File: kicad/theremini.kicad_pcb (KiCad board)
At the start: 2 copper layers, 2 parts, among them U1 VL53L0CXV0DH/1, U2 VL53L0CXV0DH/1

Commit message: Add libraries
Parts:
- removed U1, U2: VL53L0CXV0DH/1, VL53L0CXV0DH1:OPTO-SMD_12P_VL53L0CXV0DH-1
- added U3: STM32L432KBUx, Package_DFN_QFN:QFN-32-1EP_5x5mm_P0.5mm_EP3.45x3.45mm, F.Cu at (3.15, 3.15)

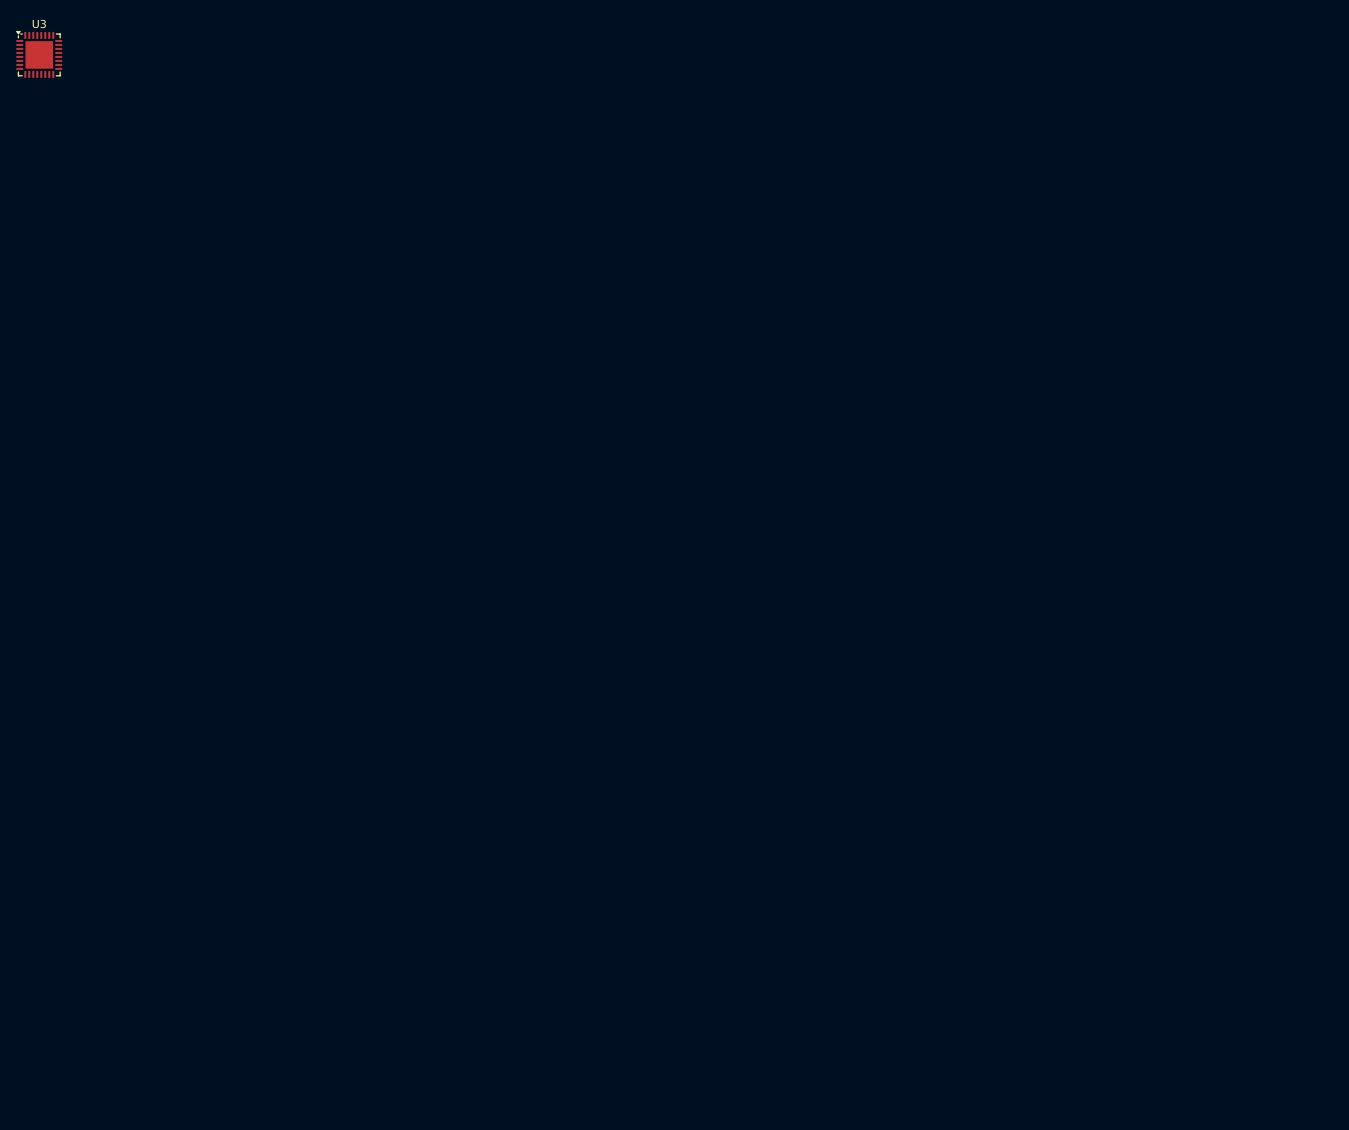
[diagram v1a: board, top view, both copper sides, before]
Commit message: Place footprints
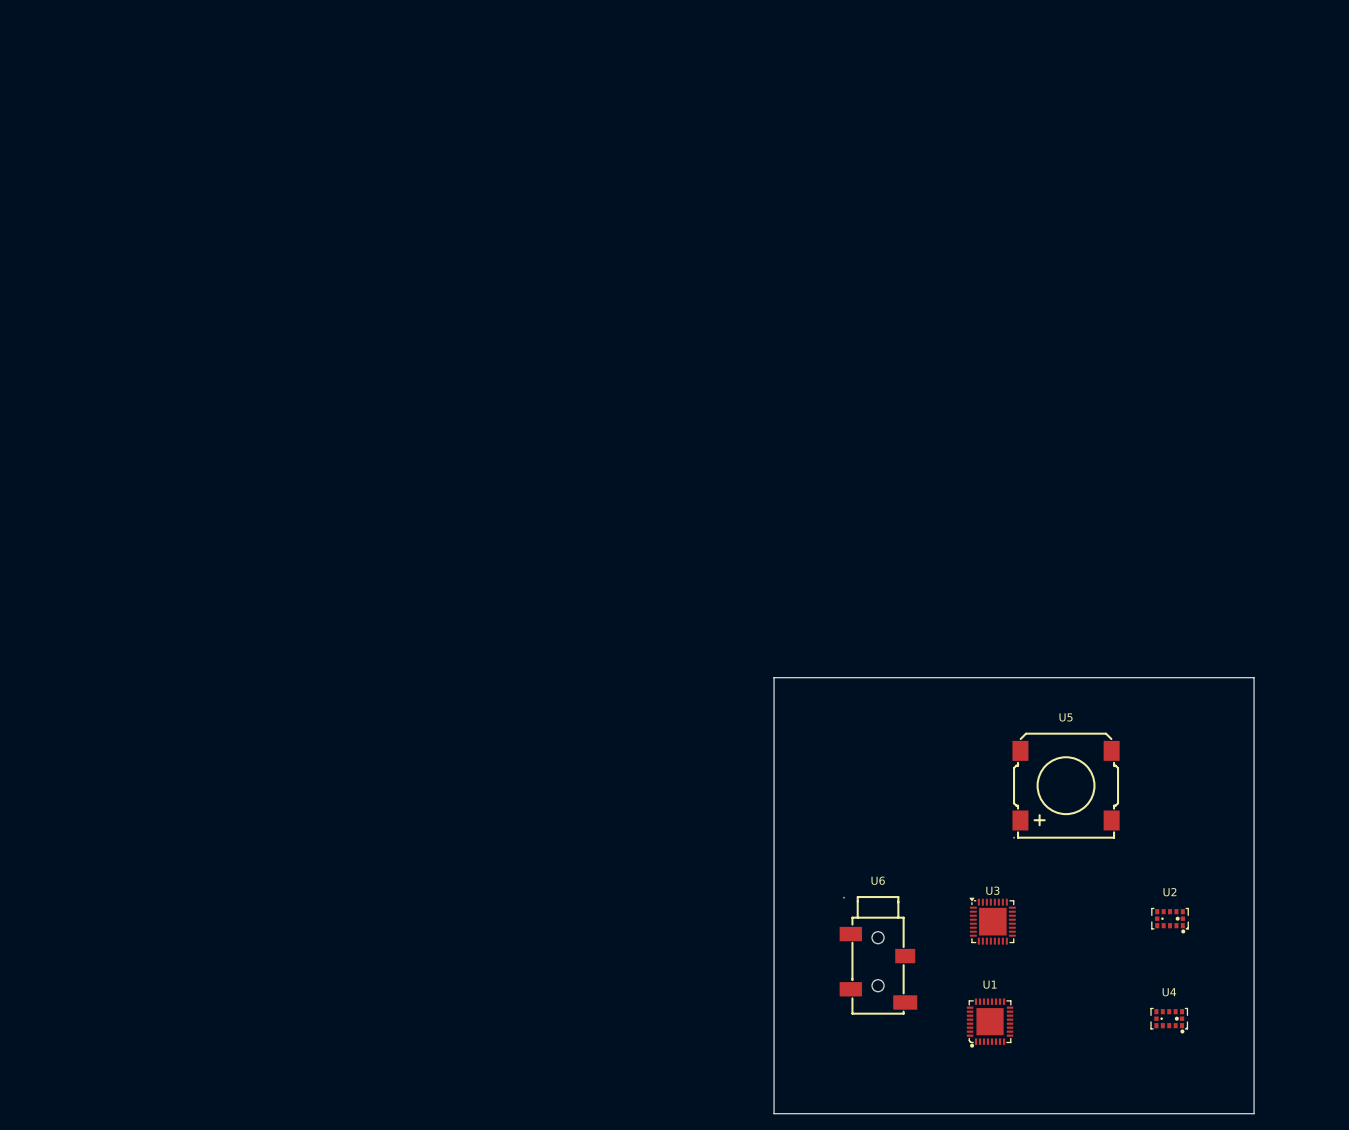
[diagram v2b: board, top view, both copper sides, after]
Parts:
- added U1: NAU88C22YG, NAU88C22YG:QFN-32_L5.0-W5.0-P0.50-BL-EP3.4, F.Cu at (122.0, 124.0)
- added U2: VL53L0CXV0DH/1, VL53L0CXV0DH1:OPTO-SMD_12P_VL53L0CXV0DH-1, F.Cu at (144.5, 111.1)
- added U4: VL53L0CXV0DH/1, VL53L0CXV0DH1:OPTO-SMD_12P_VL53L0CXV0DH-1, F.Cu at (144.4, 123.6)
- added U5: KLJ-01304T-08R07W, KLJ-01304T-08R07W:BUZ-SMD_4P-L13.0-W13.0-P11.4-BL, F.Cu at (131.5, 94.5)
- added U6: PJ-327C-4A, PJ-327C-4A:AUDIO-SMD_PJ-327C-4A, F.Cu at (108.0, 117.3)
- moved U3 161.1 mm to (122.3, 111.5)
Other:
- board outline added: 60 x 54.5 mm

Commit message: added things
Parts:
- removed U3: STM32L432KBUx, Package_DFN_QFN:QFN-32-1EP_5x5mm_P0.5mm_EP3.45x3.45mm
- added U7: STM32L432KBU6TR, STM32L432KBU6TR:UFQFPN-32_L5.0-W5.0-P0.50-TL-EP3.5, F.Cu at (123.0, 110.7)

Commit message: Connected things
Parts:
- added C1: 10u, Capacitor_SMD:C_0402_1005Metric, F.Cu at (100.7, 85.9)
- added C10: 100n, Capacitor_SMD:C_0402_1005Metric, F.Cu at (108.7, 88.4)
- added C11: 100n, Capacitor_SMD:C_0402_1005Metric, F.Cu at (108.7, 90.9)
- added C12: 15p, Capacitor_SMD:C_0402_1005Metric, F.Cu at (108.7, 93.4)
- added C2: 10u, Capacitor_SMD:C_0402_1005Metric, F.Cu at (100.7, 88.4)
- added C3: 10u, Capacitor_SMD:C_0402_1005Metric, F.Cu at (100.7, 90.9)
- added C4: 1n, Capacitor_SMD:C_0402_1005Metric, F.Cu at (100.7, 93.4)
- added C5: 4u7, Capacitor_SMD:C_0402_1005Metric, F.Cu at (104.7, 85.9)
- added C6: 100n, Capacitor_SMD:C_0402_1005Metric, F.Cu at (104.7, 88.4)
- added C7: 100n, Capacitor_SMD:C_0402_1005Metric, F.Cu at (104.7, 90.9)
- added C8: 10n, Capacitor_SMD:C_0402_1005Metric, F.Cu at (104.7, 93.4)
- added C9: 1u, Capacitor_SMD:C_0402_1005Metric, F.Cu at (108.7, 85.9)
- added L1: 1.5u, Inductor_SMD:L_0201_0603Metric, F.Cu at (111.9, 85.5)
- added L2: BLM15AG601SN1D, BLM15AG601SN1D:L0402, F.Cu at (112.4, 91.0)
- added R1: 1M, Resistor_SMD:R_0201_0603Metric, F.Cu at (111.9, 87.3)
- added R2: 10k, Resistor_SMD:R_0201_0603Metric, F.Cu at (111.9, 89.0)
- added U3: TPS63051YFFR, TPS63051YFFR:DSBGA-12_L1.6-W1.2-R3-C4-P0.40-BL, F.Cu at (110.9, 100.6)
- added U9: TYPE-C16PIN, TYPE-C16PIN:USB-C-SMD_TYPE-C16PIN, F.Cu at (104.0, 98.1)
- added X1: OT32258MJBA4SL, OT32258MJBA4SL:OSC-SMD_4P-L3.2-W2.5-BL, F.Cu at (112.2, 96.9)
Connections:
- U7 pad 1: unconnected-(U7-VDD-Pad1) -> +3.3V
- U7 pad 17: unconnected-(U7-VDD-Pad17) -> +3.3V
- U7 pad 31: unconnected-(U7-PH3/BOOT0-Pad31) -> Net-(U7-PH3/BOOT0)
- U7 pad 32: unconnected-(U7-VSS-Pad32) -> GND
- U7 pad 4: unconnected-(U7-NRST-Pad4) -> NRST
- U7 pad 5: unconnected-(U7-VDDA/VREF+-Pad5) -> VDDA
- U7 pad 6: unconnected-(U7-PA0/CK_IN-Pad6) -> XTAL OUT
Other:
- board size 60 x 54.5 mm -> 87 x 76 mm

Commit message: just update ig
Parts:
- U4, U5, U7, U9: moved to B.Cu
- moved U4 15.8 mm to (130.6, 116.0), turned to 180 degrees
- moved U9 11.7 mm to (93.0, 102.0), turned to 180 degrees
- moved U7 2.85 mm to (120.8, 109.0), turned to 180 degrees
- moved U5 2.50 mm to (129.5, 93.0), turned to 180 degrees
